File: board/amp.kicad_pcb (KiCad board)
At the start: 2 copper layers, 29.8 x 54.6 mm, 34 parts, among them J1 GUITAR_IN, J2 POWER, J3 OUT, SW2 SW_DIST, U1 TL071

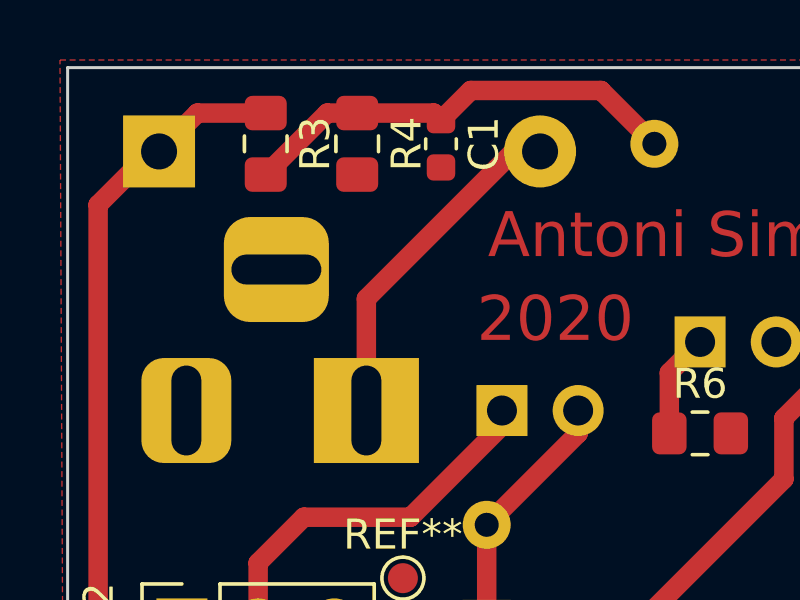
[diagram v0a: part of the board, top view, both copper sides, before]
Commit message: Fix board, README corrections
Reverse power jack polarity (make it center-negative), fix typos and
other mistakes in README
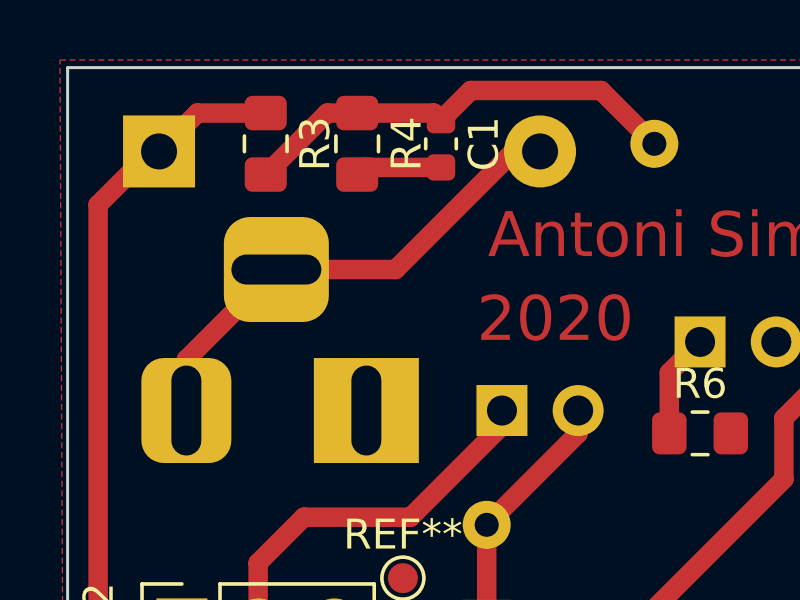
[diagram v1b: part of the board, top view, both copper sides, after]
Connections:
- J1 pad SN: (no net) -> Net-(J1-PadSN)
- J1 pad TN: (no net) -> Net-(J1-PadTN)
- J2 pad 1: Net-(D1-Pad2) -> GND
- J2 pad 2: GND -> Net-(D1-Pad2)
- J2 pad 3: GND -> Net-(D1-Pad2)
- J3 pad SN: (no net) -> Net-(J3-PadSN)
- J3 pad TN: (no net) -> Net-(J3-PadTN)
- U1 pad 1: (no net) -> Net-(U1-Pad1)
- U1 pad 5: (no net) -> Net-(U1-Pad5)
- U1 pad 8: (no net) -> Net-(U1-Pad8)
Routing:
- net Net-(D1-Pad2): track 11.6 -> 16.4 mm
- net GND: track 0.00 -> 2.89 mm
